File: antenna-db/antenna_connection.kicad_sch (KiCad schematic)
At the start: 4 parts

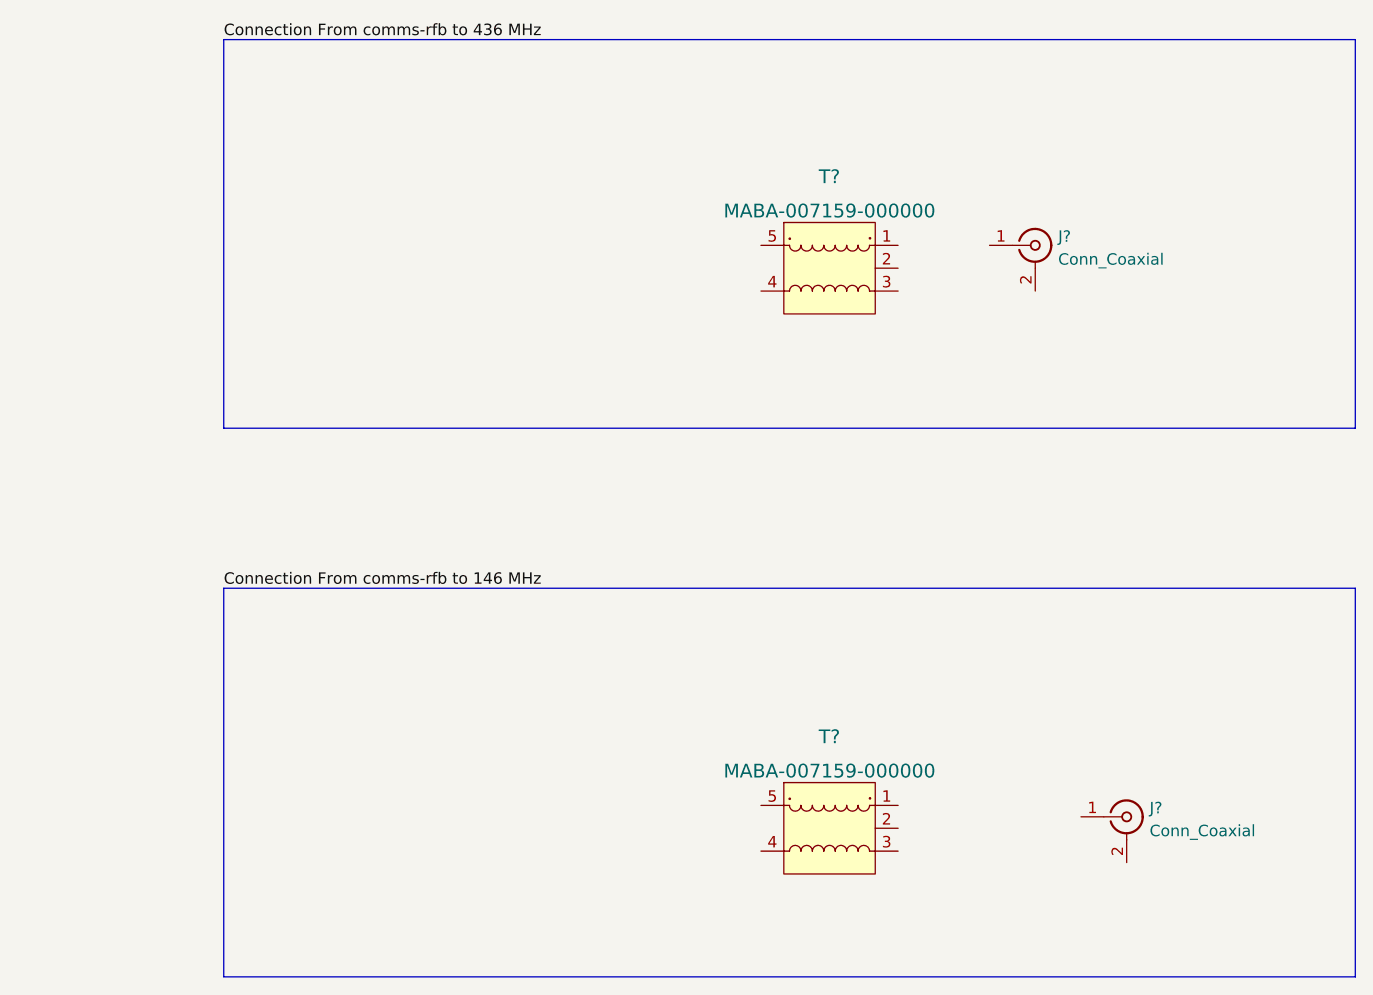
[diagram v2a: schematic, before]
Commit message: added balun connection
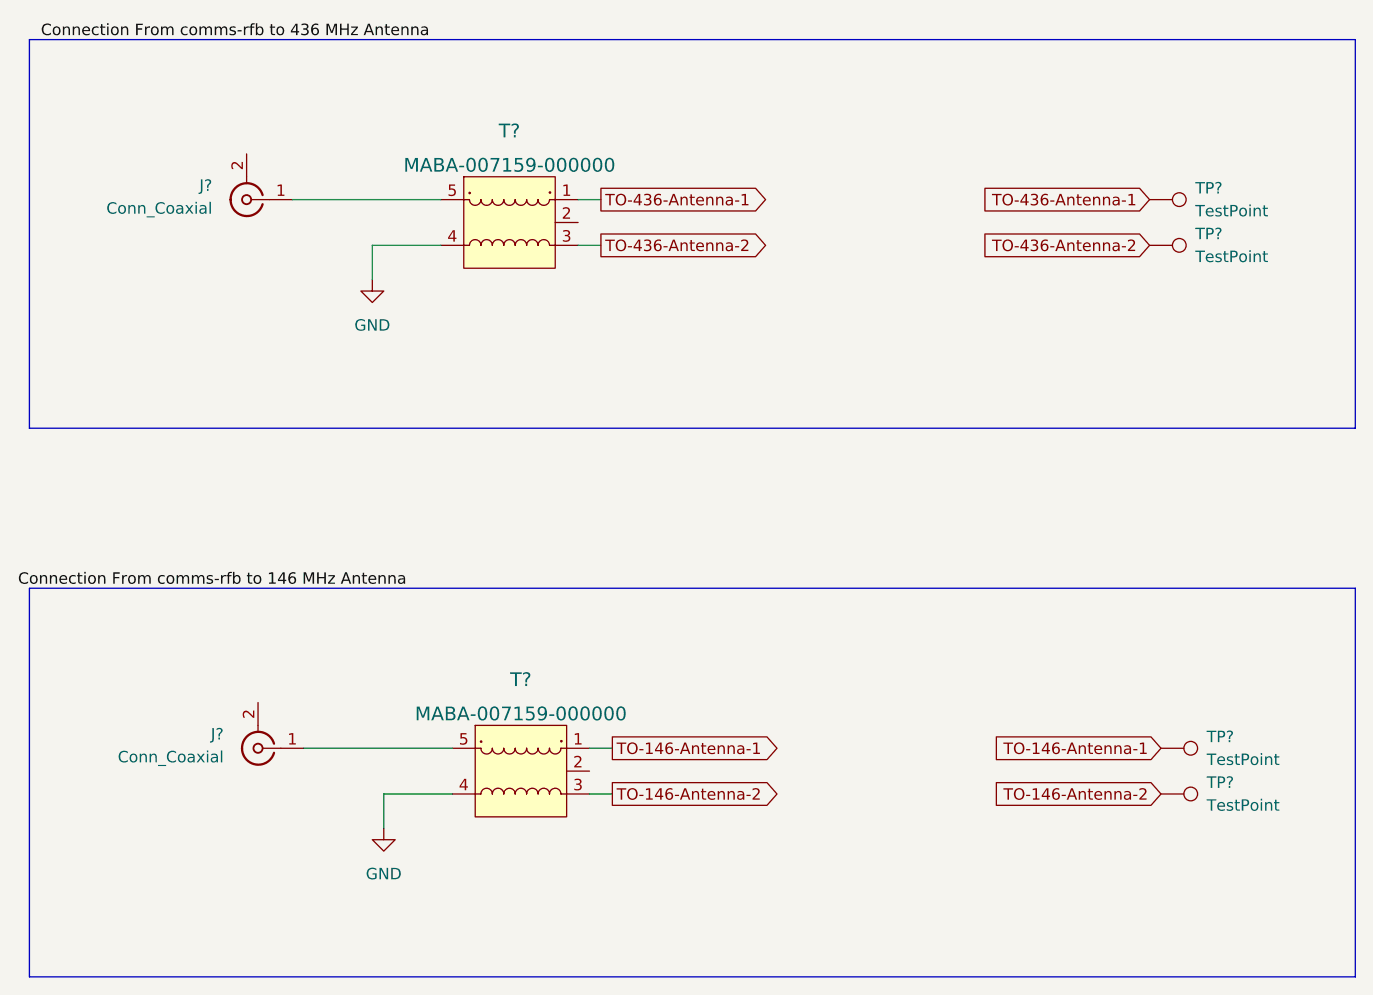
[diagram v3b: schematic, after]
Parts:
- removed J?: Conn_Coaxial, symbol Connector:Conn_Coaxial
- removed T?: MABA-007159-000000, digikey-footprints:SMD-5-6_3.83x2.79mm, symbol dk_Balun:MABA-007159-000000
- added J?: Conn_Coaxial, symbol Connector:Conn_Coaxial
- added T?: MABA-007159-000000, digikey-footprints:SMD-5-6_3.83x2.79mm, symbol dk_Balun:MABA-007159-000000
- added TP? (x4): TestPoint, symbol Connector:TestPoint
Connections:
- net at J?.1 (In): now also T?.5
- net TO-436-Antenna-1: now reaches T?.1
- net TO-436-Antenna-1: now also TP?.1
- net TO-436-Antenna-2: now reaches T?.3
- net TO-436-Antenna-2: now also TP?.1
- net GND: now reaches T?.4
- net GND: now also T?.4
- new net: J?.1 (In), T?.5
- new net TO-146-Antenna-1: T?.1, TP?.1
- new net TO-146-Antenna-2: T?.3, TP?.1
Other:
- moved on the sheet: J?, T?
